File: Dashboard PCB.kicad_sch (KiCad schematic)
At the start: 40 parts, among them J1 Controls_Leader_Export_02x06, J2 Conn_02x03_CAN, J4 FAN_CTRL_01x02, J5 Horn_In_01x02, J6 Horn_Out_01x02, J7 Conn_02x03_CAN, J8 Supp_Out, J9 Supp_In

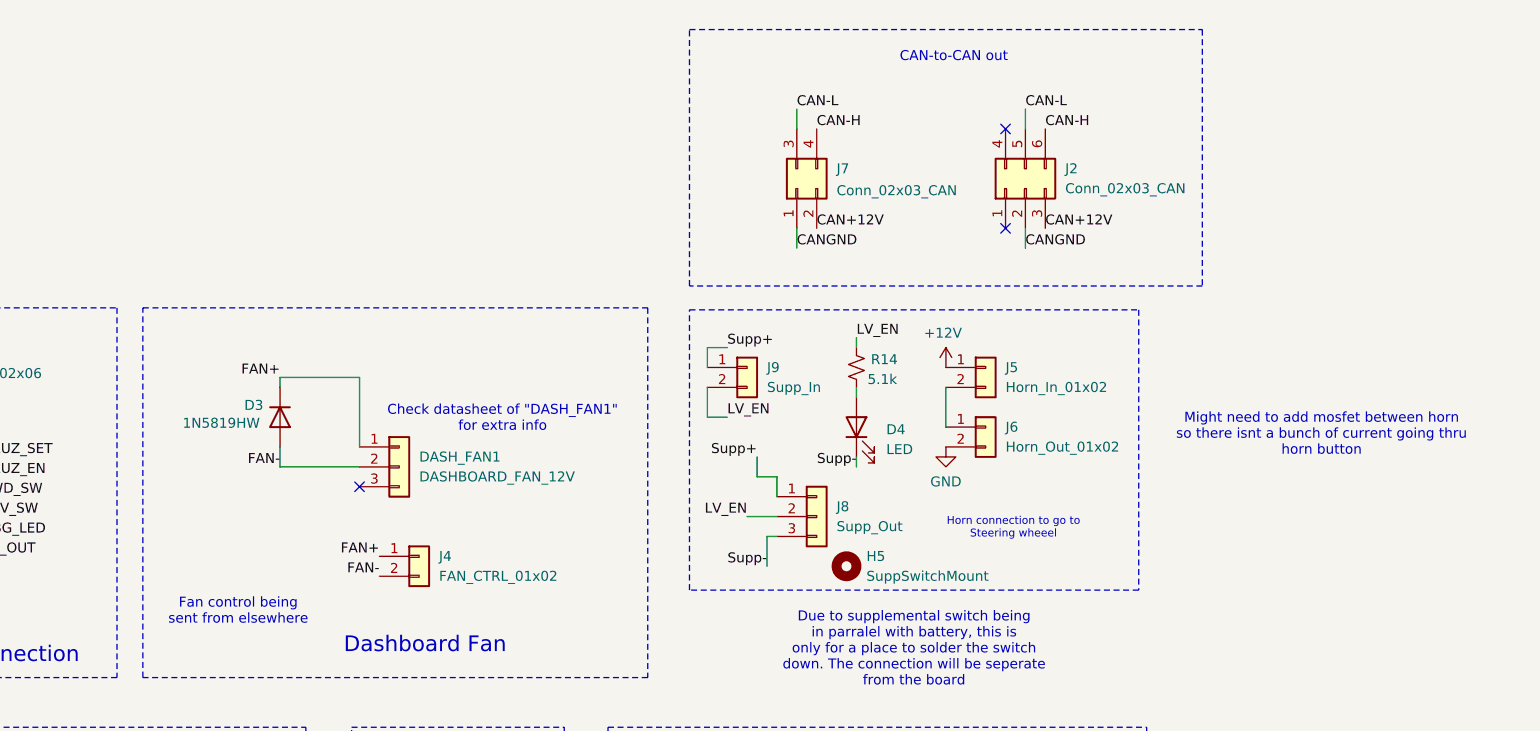
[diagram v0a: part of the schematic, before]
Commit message: Johnathan
Added FET for horn, fixed other stuff, etc
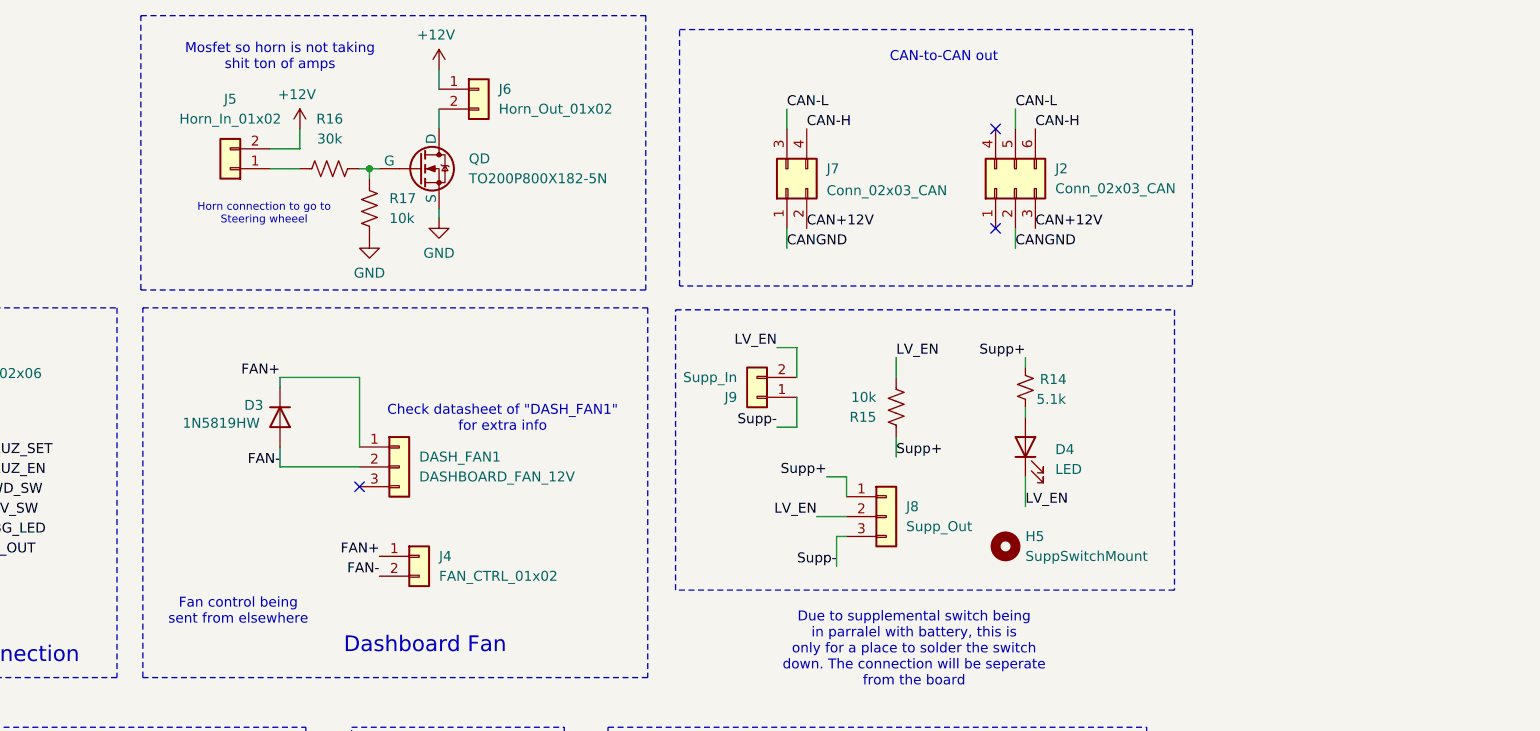
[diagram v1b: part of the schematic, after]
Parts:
- added QD: TO200P800X182-5N, Footprints:TO200P800X182-5N, symbol Simulation_SPICE:NMOS
- added R15, R17: 10k, Resistor_SMD:R_0805_2012Metric_Pad1.20x1.40mm_HandSolder, symbol Device:R_US
- added R16: 30k, Resistor_SMD:R_0805_2012Metric_Pad1.20x1.40mm_HandSolder, symbol Device:R_US
- BPS_HZD_LED1, D4, Heartbeat_LED1, LFT_LED1, RT_LED1: footprint LED_SMD:LED_0805_2012Metric -> LED_SMD:LED_0805_2012Metric_Pad1.15x1.40mm_HandSolder
- C10, C11: footprint Capacitor_SMD:C_0805_2012Metric -> Capacitor_SMD:C_0805_2012Metric_Pad1.18x1.45mm_HandSolder
- R10, R11, R12, R13, R14: footprint Resistor_SMD:R_0805_2012Metric -> Resistor_SMD:R_0805_2012Metric_Pad1.20x1.40mm_HandSolder
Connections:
- net +12V: now also J5.2 (Pin_2), J6.1 (Pin_1); no longer J5.1 (Pin_1)
- net GND: now also QD.3 (S), R17.2; no longer J6.2 (Pin_2)
- net LV_EN: now also D4.1 (K), R15.2; no longer R14.1
- net Supp+: now also R14.1, R15.1; no longer J9.1 (Pin_1)
- net Supp-: now also J9.1 (Pin_1); no longer D4.1 (K)
- new net: QD.2 (G), R16.1, R17.1
- new net: J5.1 (Pin_1), R16.2
- new net: J6.2 (Pin_2), QD.1 (D)
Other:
- note added: "Mosfet so horn is not taking shit ton of amps"
- note removed: "Might need to add mosfet between horn so there isnt a bunch of current going thru horn button"
- moved on the sheet: D4, H5, J2, J5, J6, J7, J8, J9, R14

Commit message: franK
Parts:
- removed R14: 5.1k, Resistor_SMD:R_0805_2012Metric_Pad1.20x1.40mm_HandSolder, symbol Device:R_Small_US
- R15: value 10k -> 5.1k
- renumbered QD to QD1
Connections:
- net LV_EN: no longer D4.1 (K)
- net Supp-: now also D4.1 (K); no longer J9.1 (Pin_1)
- net Led: now reaches D4.2 (A)
- net Led: now also J9.1 (Pin_1)
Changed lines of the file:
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@@
 	(wire
 		(pts
-			(xy 241.3 68.58) (xy 241.3 67.31)
-		)
-		(stroke
-			(width 0)
-			(type default)
-		)
-	)
-	(wire
-		(pts
 			(xy 102.87 128.27) (xy 102.87 129.54)
 		)
@@
 	(wire
 		(pts
-			(xy 241.3 73.66) (xy 241.3 74.93)
+			(xy 241.3 72.39) (xy 241.3 74.93)
 		)
 		(stroke
@@
 		)
 	)
-	(label "Supp-"
+	(label "Led"
 		(at 209.55 76.2 180)
 		(fields_autoplaced yes)
@@
 		)
 	)
-	(label "LV_EN"
-		(at 241.3 86.36 0)
-		(fields_autoplaced yes)
-		(effects
-			(font
-				(size 1.27 1.27)
-			)
-			(justify left bottom)
-		)
-	)
 	(label "REV_SW"
 		(at 54.61 97.79 0)
@@
 		)
 	)
-	(label "Supp+"
-		(at 241.3 67.31 180)
+	(label "FWD_SW"
+		(at 107.95 85.09 0)
 		(fields_autoplaced yes)
 		(effects
@@
 				(size 1.27 1.27)
 			)
-			(justify right bottom)
+			(justify left bottom)
 		)
 	)
-	(label "FWD_SW"
-		(at 107.95 85.09 0)
+	(label "Led"
+		(at 241.3 72.39 0)
 		(fields_autoplaced yes)
 		(effects
@@
 		)
 	)
+	(label "Supp-"
+		(at 241.3 86.36 180)
+		(fields_autoplaced yes)
+		(effects
+			(font
+				(size 1.27 1.27)
+			)
+			(justify right bottom)
+		)
+	)
 	(label "IGN_MTR"
 		(at 54.61 90.17 0)
@@
 		(dnp no)
 		(fields_autoplaced yes)
-		(property "Reference" "QD"
+		(property "Reference" "QD1"
 			(at 170.18 41.9099 0)
 			(effects
@@
 			(project ""
 				(path "/db66d699-14af-49af-adc9-07d31d38aebd"
-					(reference "QD")
+					(reference "QD1")
 					(unit 1)
 				)
@@
 		(fields_autoplaced yes)
 		(property "Reference" "R15"
-			(at 222.25 74.9301 0)
+			(at 227.33 72.3899 0)
 			(effects
 				(font
 					(size 1.27 1.27)
 				)
-				(justify left)
+				(justify right)
 			)
 		)
-		(property "Value" "10k"
-			(at 222.25 72.3901 0)
+		(property "Value" "5.1k"
+			(at 227.33 74.9299 0)
 			(effects
 				(font
 					(size 1.27 1.27)
 				)
-				(justify left)
+				(justify right)
 			)
 		)
@@
 					(unit 1)
 				)
-			)
-		)
-	)
-	(symbol
-		(lib_id "Device:R_Small_US")
-		(at 241.3 71.12 0)
-		(unit 1)
-		(exclude_from_sim no)
-		(in_bom yes)
-		(on_board yes)
-		(dnp no)
-		(property "Reference" "R14"
-			(at 244.856 70.104 0)
-			(effects
-				(font
-					(size 1.27 1.27)
-				)
-			)
-		)
-		(property "Value" "5.1k"
-			(at 244.602 72.644 0)
-			(effects
-				(font
-					(size 1.27 1.27)
-				)
-			)
-		)
-		(property "Footprint" "Resistor_SMD:R_0805_2012Metric_Pad1.20x1.40mm_HandSolder"
-			(at 241.3 71.12 0)
-			(effects
-				(font
-					(size 1.27 1.27)
-				)
-				(hide yes)
-			)
-		)
-		(property "Datasheet" "~"
-			(at 241.3 71.12 0)
-			(effects
-				(font
-					(size 1.27 1.27)
-				)
-				(hide yes)
-			)
-		)
-		(property "Description" "Resistor, small US symbol"
-			(at 241.3 71.12 0)
-			(effects
-				(font
-					(size 1.27 1.27)
-				)
-				(hide yes)
-			)
-		)
-		(property "P/N" "CRCW0805100RFKEAHP"
-			(at 241.3 71.12 90)
-			(effects
-				(font
-					(size 1.27 1.27)
-				)
-				(hide yes)
-			)
-		)
-		(property "Field5" ""
-			(at 241.3 71.12 0)
-			(effects
-				(font
-					(size 1.27 1.27)
-				)
-				(hide yes)
-			)
-		)
-		(pin "1"
-		)
-		(pin "2"
-		)
-		(instances
-			(project "Dashboard PCB"
-				(path "/db66d699-14af-49af-adc9-07d31d38aebd"
-					(reference "R14")
-					(unit 1)
-				)

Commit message: Nuked some thigns
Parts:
- removed D3: 1N5819HW, Diode_SMD:D_SOD-123, symbol Device:D
- removed DASH_FAN1: DASHBOARD_FAN_12V, Connector_Molex:Molex_Micro-Fit_3.0_43650-0300_1x03_P3.00mm_Horizontal, symbol Connector_Generic:Conn_01x03
- removed FAN_CTRL1: TestPoint, TestPoint:TestPoint_Pad_1.0x1.0mm, symbol Connector:TestPoint
- removed J2: Conn_02x03_CAN, Connector_Molex:Molex_Micro-Fit_3.0_43045-0600_2x03_P3.00mm_Horizontal, symbol Connector_Generic:Conn_02x03_Top_Bottom
- removed J4: FAN_CTRL_01x02, Connector_Molex:Molex_Micro-Fit_3.0_43650-0200_1x02_P3.00mm_Horizontal, symbol Connector_Generic:Conn_01x02
- removed J7: Conn_02x03_CAN, Connector_Molex:Molex_Micro-Fit_3.0_43045-0400_2x02_P3.00mm_Horizontal, symbol Connector_Generic:Conn_02x02_Top_Bottom
- added 12V_PWR1: SMD_0805, LED_SMD:LED_0805_2012Metric_Pad1.15x1.40mm_HandSolder, symbol Device:LED
- added LV_EN1, SUPP+1, SUPP-1: TestPoint, TestPoint:TestPoint_Pad_1.0x1.0mm, symbol Connector:TestPoint
- added R14: 5.1k, Resistor_SMD:R_0805_2012Metric_Pad1.20x1.40mm_HandSolder, symbol Device:R_Small_US
- R13: value HZD_RES_VAL -> 5.1k
- renumbered QD1 to Q1
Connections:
- net +12V: now also R14.1
- net GND: now also 12V_PWR1.1 (K)
- net LV_EN: now also LV_EN1.1
- net Supp+: now also SUPP+1.1
- net Supp-: now also SUPP-1.1
- new net: 12V_PWR1.2 (A), R14.2
- no-connect marks 3 -> 0
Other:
- note removed: "CAN-to-CAN out"
- note removed: "Check datasheet of "DASH_FAN1" for extra info"
- note removed: "Dashboard Fan"
- note removed: "Fan control being sent from elsewhere"
- moved on the sheet: +12V1, BPS_HZD1, BPS_HZD_LED1, C10, C11, CRUZ_EN1, CRUZ_SET1, D4, DBG_LED1, FWD_SW1, GND1, Heartbeat_LED1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

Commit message: Quick change (fuse not added yet)
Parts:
- added F1: Fuse, symbol Device:Fuse
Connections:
- net +12V: now also F1.1; no longer J1.1 (Pin_1)
- new net: F1.2, J1.1 (Pin_1)
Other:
- note added: "Not impl yet"
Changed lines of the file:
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@@
 	(wire
 		(pts
+			(xy 95.25 74.93) (xy 95.25 78.74)
+		)
+		(stroke
+			(width 0)
+			(type default)
+		)
+	)
+	(wire
+		(pts
 			(xy 212.09 66.04) (xy 212.09 69.85)
 		)
@@
 	(wire
 		(pts
+			(xy 85.09 74.93) (xy 82.55 74.93)
+		)
+		(stroke
+			(width 0)
+			(type default)
+		)
+	)
+	(wire
+		(pts
 			(xy 229.87 148.59) (xy 229.87 147.32)
 		)
@@
 	(wire
 		(pts
+			(xy 82.55 74.93) (xy 82.55 71.12)
+		)
+		(stroke
+			(width 0)
+			(type default)
+		)
+	)
+	(wire
+		(pts
 			(xy 224.79 80.01) (xy 224.79 77.47)
 		)
@@
 	(wire
 		(pts
+			(xy 92.71 74.93) (xy 95.25 74.93)
+		)
+		(stroke
+			(width 0)
+			(type default)
+		)
+	)
+	(wire
+		(pts
 			(xy 148.59 74.93) (xy 148.59 77.47)
 		)
@@
 	(wire
 		(pts
-			(xy 95.25 78.74) (xy 95.25 77.47)
-		)
-		(stroke
-			(width 0)
-			(type default)
-		)
-	)
-	(wire
-		(pts
 			(xy 209.55 76.2) (xy 212.09 76.2)
 		)
@@
 		)
 	)
+	(text "Not impl yet"
+		(exclude_from_sim no)
+		(at 98.552 70.866 0)
+		(effects
+			(font
+				(size 1 1)
+			)
+		)
+	)
 	(text "Note: All logic is 12V"
 		(exclude_from_sim no)
@@
 	(symbol
 		(lib_id "power:+3.3V")
-		(at 95.25 77.47 0)
+		(at 82.55 71.12 0)
 		(mirror y)
 		(unit 1)
@@
 		(dnp no)
 		(property "Reference" "#PWR028"
-			(at 95.25 81.28 0)
+			(at 82.55 74.93 0)
 			(effects
 				(font
@@
 		)
 		(property "Value" "+12V"
-			(at 94.869 73.0758 0)
+			(at 82.169 66.7258 0)
 			(effects
 				(font
@@
 		)
 		(property "Footprint" ""
-			(at 95.25 77.47 0)
+			(at 82.55 71.12 0)
 			(effects
 				(font
@@
 		)
 		(property "Datasheet" ""
-			(at 95.25 77.47 0)
+			(at 82.55 71.12 0)
 			(effects
 				(font
@@
 		)
 		(property "Description" "Power symbol creates a global label with name \"+3.3V\""
-			(at 95.25 77.47 0)
+			(at 82.55 71.12 0)
 			(effects
 				(font
@@
 	)
 	(symbol
+		(lib_id "Device:Fuse")
+		(at 88.9 74.93 90)
+		(unit 1)
+		(exclude_from_sim no)
+		(in_bom yes)
+		(on_board yes)
+		(dnp no)
+		(fields_autoplaced yes)
+		(property "Reference" "F1"
+			(at 88.9 68.58 90)
+			(effects
+				(font
+					(size 1.27 1.27)
+				)
+			)
+		)
+		(property "Value" "Fuse"
+			(at 88.9 71.12 90)
+			(effects
+				(font
+					(size 1.27 1.27)
+				)
+			)
+		)
+		(property "Footprint" ""
+			(at 88.9 76.708 90)
+			(effects
+				(font
+					(size 1.27 1.27)
+				)
+				(hide yes)
+			)
+		)
+		(property "Datasheet" "~"
+			(at 88.9 74.93 0)
+			(effects
+				(font
+					(size 1.27 1.27)
+				)
+				(hide yes)
+			)
+		)
+		(property "Description" "Fuse"
+			(at 88.9 74.93 0)
+			(effects
+				(font
+					(size 1.27 1.27)
+				)
+				(hide yes)
+			)
+		)
+		(pin "1"
+		)
+		(pin "2"
+		)
+		(instances
+			(project ""
+				(path "/db66d699-14af-49af-adc9-07d31d38aebd"
+					(reference "F1")
+					(unit 1)
+				)
+			)
+		)
+	)
+	(symbol
 		(lib_id "power:GND")
 		(at 95.25 95.25 0)
@@
 		(dnp no)
 		(property "Reference" "J1"
-			(at 102.108 66.802 0)
+			(at 101.346 62.738 0)
 			(effects
 				(font
@@
 		)
 		(property "Value" "Controls_Leader_Export_02x06"
-			(at 102.108 69.342 0)
+			(at 101.346 65.278 0)
 			(effects
 				(font

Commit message: ravi and lakshay are so mean to me
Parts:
- added D3: BZT52-B12-QX, Footprints:BZT52B12QX, symbol Device:D_Zener
- added Q2: Q_PMOS_GDS, Package_TO_SOT_SMD:SOT-23-3, symbol Device:Q_PMOS_GDS
- added R18: 100k, Resistor_SMD:R_0805_2012Metric_Pad1.20x1.40mm_HandSolder, symbol Device:R_US
- F1: footprint (none) -> Footprints:3588; P/N (none) -> MF-PSHT020KX-2
- renumbered D4 to SUPP1
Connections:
- net GND: now also R18.1
- net at F1.2: now also D3.1 (K), Q2.2 (D); no longer J1.1 (Pin_1)
- new net: D3.2 (A), Q2.1 (G), R18.2
- new net PWR: J1.1 (Pin_1), Q2.3 (S)
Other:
- note added: "Reverse Polarity Protection"

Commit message: added stuff
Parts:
- D3: P/N (none) -> BZT52-B12-QX
- Q1: P/N (none) -> TO200P800X182-5N
- Q2: P/N (none) -> Reverse polarity PMOS
- R16: P/N (none) -> 30k res
- R17: P/N (none) -> CRCW080510K0FKEAC
- R18: P/N (none) -> 100k res

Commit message: update
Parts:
- Q1: P/N TO200P800X182-5N -> SQJQ142E-T1_GE3
- Q2: P/N Reverse polarity PMOS -> PMV35EPER
- R18: P/N 100k res -> At pikel
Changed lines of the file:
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@@
 			)
 		)
-		(property "P/N" "TO200P800X182-5N"
+		(property "P/N" "SQJQ142E-T1_GE3"
 			(at 163.83 80.01 0)
 			(effects
@@
 			)
 		)
-		(property "P/N" "Reverse polarity PMOS"
+		(property "P/N" "PMV35EPER"
 			(at 96.52 41.91 90)
 			(effects
@@
 		(property "Link" ""
 			(at 96.52 41.91 0)
+			(effects
+				(font
+					(size 1.27 1.27)
+				)
+				(hide yes)
+			)
+		)
+		(property "Field7" ""
+			(at 96.52 41.91 90)
 			(effects
 				(font
@@
 			)
 		)
-		(property "P/N" "100k res"
+		(property "P/N" "At pikel"
 			(at 90.17 49.53 90)
 			(effects

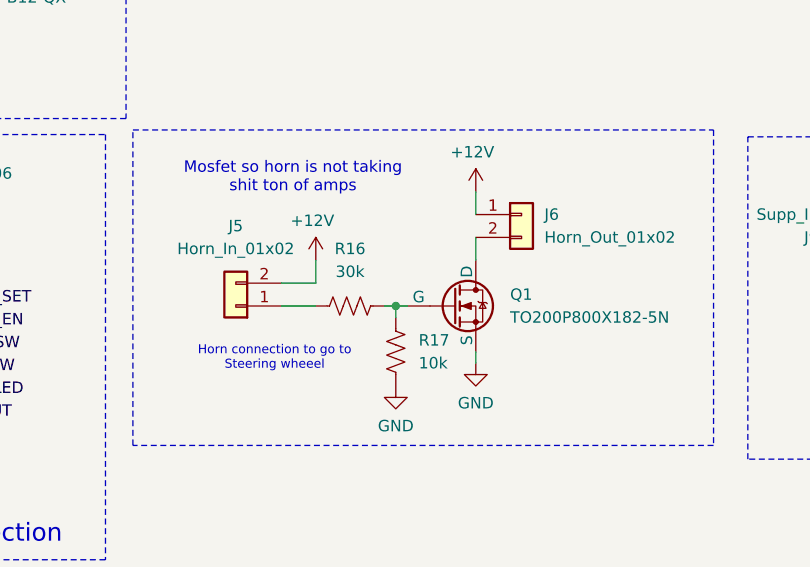
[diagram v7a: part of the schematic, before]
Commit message: added flyback and made supp hole bigger
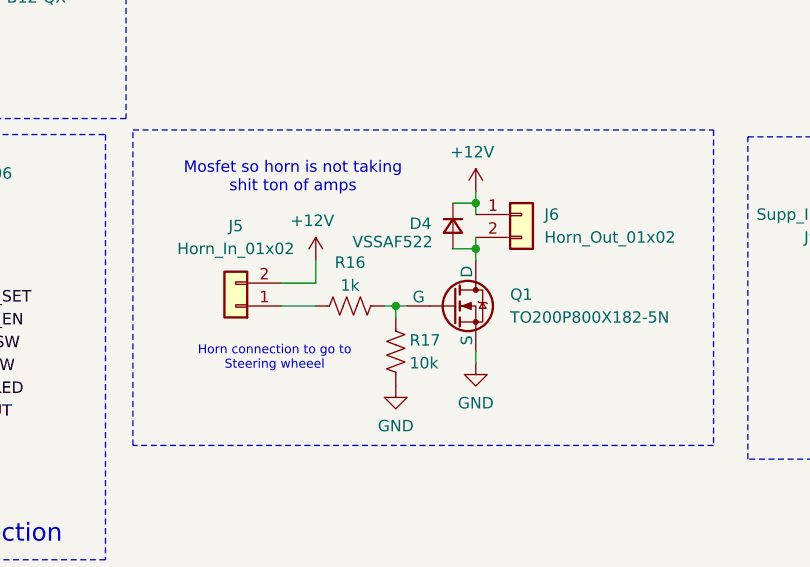
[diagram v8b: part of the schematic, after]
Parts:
- added D4: VSSAF522, Footprints:DO-221AC, symbol Device:D_Small
- R16: value 30k -> 1k
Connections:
- net +12V: now also D4.C (K)
- net at J6.2 (Pin_2), Q1.1 (D): now also D4.A
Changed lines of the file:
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@@
 	)
 	(junction
+		(at 166.37 68.58)
+		(diameter 0)
+		(color 0 0 0 0)
+	)
+	(junction
 		(at 157.48 80.01)
 		(diameter 0)
@@
 		(color 0 0 0 0)
 	)
+	(junction
+		(at 166.37 73.66)
+		(diameter 0)
+		(color 0 0 0 0)
+	)
 	(wire
 		(pts
@@
 	(wire
 		(pts
+			(xy 163.83 68.58) (xy 166.37 68.58)
+		)
+		(stroke
+			(width 0)
+			(type default)
+		)
+	)
+	(wire
+		(pts
 			(xy 212.09 76.2) (xy 212.09 72.39)
 		)
@@
 	(wire
 		(pts
-			(xy 166.37 72.39) (xy 166.37 74.93)
+			(xy 166.37 72.39) (xy 166.37 73.66)
 		)
 		(stroke
@@
 	(wire
 		(pts
-			(xy 166.37 67.31) (xy 166.37 69.85)
+			(xy 166.37 67.31) (xy 166.37 68.58)
 		)
 		(stroke
@@
 	(wire
 		(pts
+			(xy 163.83 73.66) (xy 166.37 73.66)
+		)
+		(stroke
+			(width 0)
+			(type default)
+		)
+	)
+	(wire
+		(pts
 			(xy 92.71 74.93) (xy 95.25 74.93)
 		)
@@
 	(wire
 		(pts
+			(xy 166.37 68.58) (xy 166.37 69.85)
+		)
+		(stroke
+			(width 0)
+			(type default)
+		)
+	)
+	(wire
+		(pts
 			(xy 218.44 82.55) (xy 215.9 82.55)
 		)
@@
 	(wire
 		(pts
+			(xy 166.37 73.66) (xy 166.37 74.93)
+		)
+		(stroke
+			(width 0)
+			(type default)
+		)
+	)
+	(wire
+		(pts
 			(xy 172.72 132.08) (xy 175.26 132.08)
 		)
@@
 		(on_board yes)
 		(dnp no)
-		(fields_autoplaced yes)
 		(property "Reference" "R17"
-			(at 160.02 83.8199 0)
+			(at 159.004 83.82 0)
 			(effects
 				(font
@@
 		)
 		(property "Value" "10k"
-			(at 160.02 86.3599 0)
+			(at 159.004 86.36 0)
 			(effects
 				(font
@@
 		(on_board yes)
 		(dnp no)
-		(fields_autoplaced yes)
 		(property "Reference" "R16"
-			(at 152.4 73.66 90)
+			(at 152.4 75.184 90)
 			(effects
 				(font
@@
 			)
 		)
-		(property "Value" "30k"
-			(at 152.4 76.2 90)
+		(property "Value" "1k"
+			(at 152.4 77.724 90)
 			(effects
 				(font
@@
 					(unit 1)
 				)
+			)
+		)
+	)
+	(symbol
+		(lib_id "Device:D_Small")
+		(at 163.83 71.12 270)
+		(unit 1)
+		(exclude_from_sim no)
+		(in_bom yes)
+		(on_board yes)
+		(dnp no)
+		(property "Reference" "D4"
+			(at 159.004 70.866 90)
+			(effects
+				(font
+					(size 1.27 1.27)
+				)
+				(justify left)
+			)
+		)
+		(property "Value" "VSSAF522"
+			(at 152.654 72.898 90)
+			(effects
+				(font
+					(size 1.27 1.27)
+				)
+				(justify left)
+			)
+		)
+		(property "Footprint" "Footprints:DO-221AC"
+			(at 161.036 55.118 90)
+			(effects
+				(font
+					(size 1.27 1.27)
+				)
+				(hide yes)
+			)
+		)
+		(property "Datasheet" "https://www.vishay.com/docs/87453/vssaf522.pdf"
+			(at 164.084 52.324 90)
+			(effects
+				(font
+					(size 1.27 1.27)
+				)
+				(hide yes)
+			)
+		)
+		(property "Description" "Diode, small symbol"
+			(at 170.434 66.548 0)
+			(effects
+				(font
+					(size 1.27 1.27)
+				)
+				(hide yes)
+			)
+		)
+		(property "Sim.Device" "D"
+			(at 167.386 76.708 0)
+			(effects
+				(font
+					(size 1.27 1.27)
+				)
+				(hide yes)
+			)
+		)
+		(property "Sim.Pins" "1=K 2=A"
+			(at 169.164 69.596 0)
+			(effects
+				(font
+					(size 1.27 1.27)
+				)
+				(hide yes)
+			)
+		)
+		(pin "A"
+		)
+		(pin "C"
+		)
+		(instances
+			(project ""
+				(path "/db66d699-14af-49af-adc9-07d31d38aebd"
+					(reference "D4")
+					(unit 1)
+				)
